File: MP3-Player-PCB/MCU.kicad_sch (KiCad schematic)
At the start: 24 parts, among them J101 Conn_ARM_SWD_TagConnect_TC2030, U101 STM32F411CEUx, Y101 8MHz

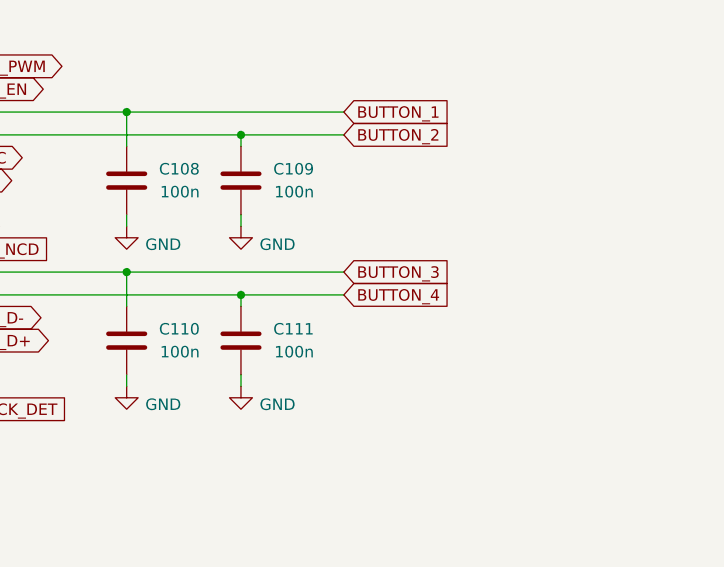
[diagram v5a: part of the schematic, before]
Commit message: Routed button gpio signals
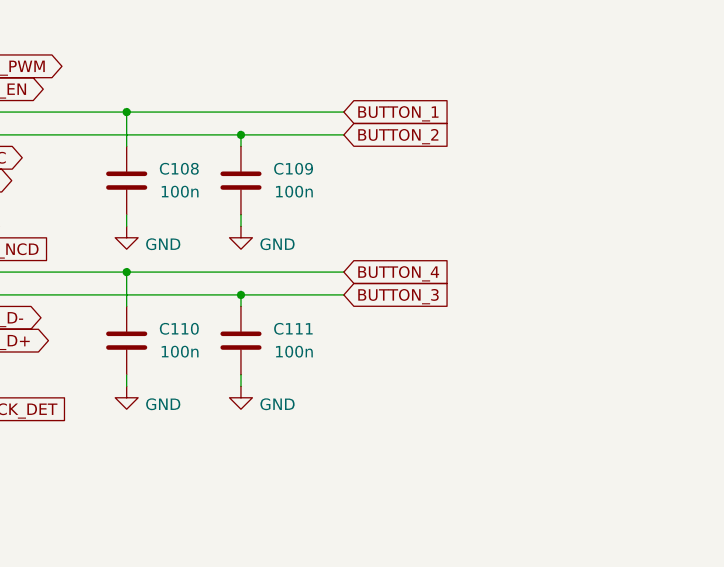
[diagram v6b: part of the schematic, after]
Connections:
- net BUTTON_3: now also C111.1, U101.31 (PA10); no longer C110.1, U101.30 (PA9)
- net BUTTON_4: now also C110.1, U101.30 (PA9); no longer C111.1, U101.31 (PA10)
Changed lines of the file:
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@@
-		)
-	)
-	(global_label "BUTTON_3"
-		(shape input)
-		(at 233.68 83.82 0)
-		(fields_autoplaced yes)
-		(effects
-			(font
-				(size 1.27 1.27)
-			)
-			(justify left)
-		)
-		(property "Intersheetrefs" "${INTERSHEET_REFS}"
-			(at 246.039 83.82 0)
-			(effects
-				(font
-					(size 1.27 1.27)
-				)
-				(justify left)
-				(hide yes)
-			)
 		)
 	)
@@
 		)
 	)
+	(global_label "SD_CARD_NCD"
+		(shape input)
+		(at 185.42 81.28 0)
+		(fields_autoplaced yes)
+		(effects
+			(font
+				(size 1.27 1.27)
+			)
+			(justify left)
+		)
+		(property "Intersheetrefs" "${INTERSHEET_REFS}"
+			(at 201.589 81.28 0)
+			(effects
+				(font
+					(size 1.27 1.27)
+				)
+				(justify left)
+				(hide yes)
+			)
+		)
+	)
+	(global_label "DAC_DIN"
+		(shape output)
+		(at 185.42 78.74 0)
+		(fields_autoplaced yes)
+		(effects
+			(font
+				(size 1.27 1.27)
+			)
+			(justify left)
+		)
+		(property "Intersheetrefs" "${INTERSHEET_REFS}"
+			(at 196.2067 78.74 0)
+			(effects
+				(font
+					(size 1.27 1.27)
+				)
+				(justify left)
+				(hide yes)
+			)
+		)
+	)
+	(global_label "DAC_GPO"
+		(shape input)
+		(at 129.54 81.28 180)
+		(fields_autoplaced yes)
+		(effects
+			(font
+				(size 1.27 1.27)
+			)
+			(justify right)
+		)
+		(property "Intersheetrefs" "${INTERSHEET_REFS}"
+			(at 118.0881 81.28 0)
+			(effects
+				(font
+					(size 1.27 1.27)
+				)
+				(justify right)
+				(hide yes)
+			)
+		)
+	)
+	(global_label "LEDS_PWR_EN"
+		(shape output)
+		(at 185.42 63.5 0)
+		(fields_autoplaced yes)
+		(effects
+			(font
+				(size 1.27 1.27)
+			)
+			(justify left)
+		)
+		(property "Intersheetrefs" "${INTERSHEET_REFS}"
+			(at 201.4679 63.5 0)
+			(effects
+				(font
+					(size 1.27 1.27)
+				)
+				(justify left)
+				(hide yes)
+			)
+		)
+	)
+	(global_label "AUDIO_JACK_DET"
+		(shape input)
+		(at 185.42 99.06 0)
+		(fields_autoplaced yes)
+		(effects
+			(font
+				(size 1.27 1.27)
+			)
+			(justify left)
+		)
+		(property "Intersheetrefs" "${INTERSHEET_REFS}"
+			(at 203.9476 99.06 0)
+			(effects
+				(font
+					(size 1.27 1.27)
+				)
+				(justify left)
+				(hide yes)
+			)
+		)
+	)
 	(global_label "BUTTON_4"
 		(shape input)
-		(at 233.68 86.36 0)
-		(fields_autoplaced yes)
-		(effects
-			(font
-				(size 1.27 1.27)
-			)
-			(justify left)
-		)
-		(property "Intersheetrefs" "${INTERSHEET_REFS}"
-			(at 246.039 86.36 0)
-			(effects
-				(font
-					(size 1.27 1.27)
-				)
-				(justify left)
-				(hide yes)
-			)
-		)
-	)
-	(global_label "SD_CARD_NCD"
-		(shape input)
-		(at 185.42 81.28 0)
-		(fields_autoplaced yes)
-		(effects
-			(font
-				(size 1.27 1.27)
-			)
-			(justify left)
-		)
-		(property "Intersheetrefs" "${INTERSHEET_REFS}"
-			(at 201.589 81.28 0)
-			(effects
-				(font
-					(size 1.27 1.27)
-				)
-				(justify left)
-				(hide yes)
-			)
-		)
-	)
-	(global_label "DAC_DIN"
-		(shape output)
-		(at 185.42 78.74 0)
-		(fields_autoplaced yes)
-		(effects
-			(font
-				(size 1.27 1.27)
-			)
-			(justify left)
-		)
-		(property "Intersheetrefs" "${INTERSHEET_REFS}"
-			(at 196.2067 78.74 0)
-			(effects
-				(font
-					(size 1.27 1.27)
-				)
-				(justify left)
-				(hide yes)
-			)
-		)
-	)
-	(global_label "DAC_GPO"
-		(shape input)
-		(at 129.54 81.28 180)
-		(fields_autoplaced yes)
-		(effects
-			(font
-				(size 1.27 1.27)
-			)
-			(justify right)
-		)
-		(property "Intersheetrefs" "${INTERSHEET_REFS}"
-			(at 118.0881 81.28 0)
-			(effects
-				(font
-					(size 1.27 1.27)
-				)
-				(justify right)
-				(hide yes)
-			)
-		)
-	)
-	(global_label "LEDS_PWR_EN"
-		(shape output)
-		(at 185.42 63.5 0)
-		(fields_autoplaced yes)
-		(effects
-			(font
-				(size 1.27 1.27)
-			)
-			(justify left)
-		)
-		(property "Intersheetrefs" "${INTERSHEET_REFS}"
-			(at 201.4679 63.5 0)
-			(effects
-				(font
-					(size 1.27 1.27)
-				)
-				(justify left)
-				(hide yes)
-			)
-		)
-	)
-	(global_label "AUDIO_JACK_DET"
-		(shape input)
-		(at 185.42 99.06 0)
-		(fields_autoplaced yes)
-		(effects
-			(font
-				(size 1.27 1.27)
-			)
-			(justify left)
-		)
-		(property "Intersheetrefs" "${INTERSHEET_REFS}"
-			(at 203.9476 99.06 0)
+		(at 233.68 83.82 0)
+		(fields_autoplaced yes)
+		(effects
+			(font
+				(size 1.27 1.27)
+			)
+			(justify left)
+		)
+		(property "Intersheetrefs" "${INTERSHEET_REFS}"
+			(at 246.039 83.82 0)
 			(effects
 				(font
@@
 				(hide yes)
 			)
+		)
+	)
+	(global_label "BUTTON_3"
+		(shape input)
+		(at 233.68 86.36 0)
+		(fields_autoplaced yes)
+		(effects
+			(font
+				(size 1.27 1.27)
+			)
+			(justify left)
+		)
+		(property "Intersheetrefs" "${INTERSHEET_REFS}"
+			(at 246.039 86.36 0)
+			(effects
+				(font
+					(size 1.27 1.27)
+				)
+				(justify left)
+				(hide yes)
+			)

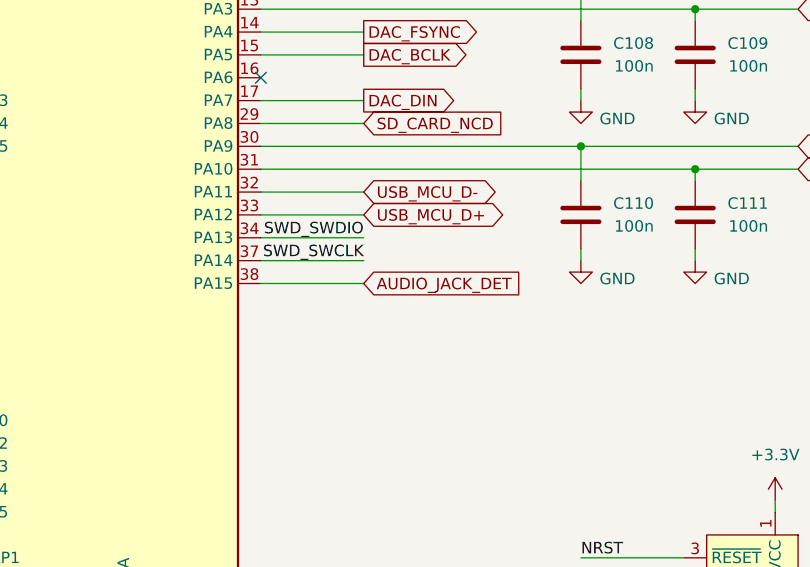
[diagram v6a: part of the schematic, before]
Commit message: Finished Audio Jack routing
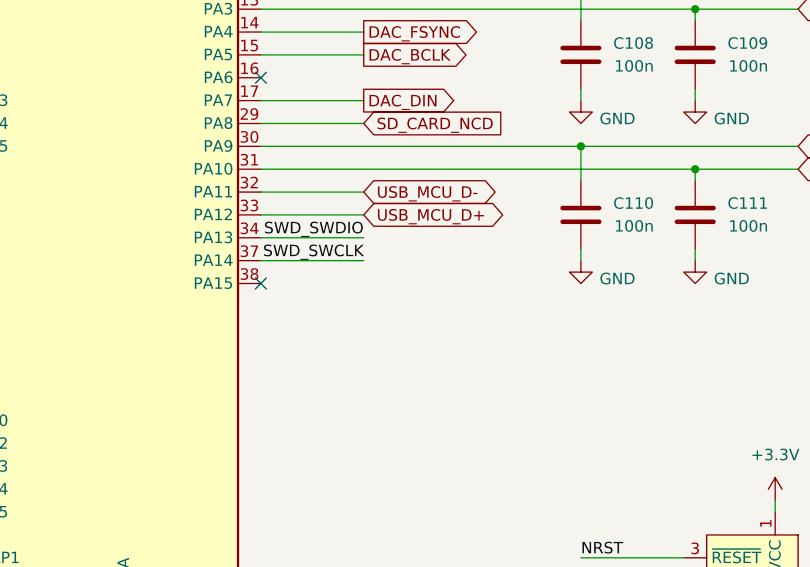
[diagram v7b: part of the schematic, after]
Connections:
- net AUDIO_JACK_DET: no longer names the net of U101.38 (PA15)
- no-connect marks 4 -> 5
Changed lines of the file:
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@@
+	)
+	(no_connect
+		(at 173.99 99.06)
 	)
 	(no_connect
@@
 		(pts
 			(xy 105.41 48.26) (xy 105.41 50.8)
-		)
-		(stroke
-			(width 0)
-			(type default)
-		)
-	)
-	(wire
-		(pts
-			(xy 185.42 99.06) (xy 173.99 99.06)
 		)
 		(stroke
@@
 			(effects
 				(font
-					(size 1.27 1.27)
-				)
-				(justify left)
-				(hide yes)
-			)
-		)
-	)
-	(global_label "AUDIO_JACK_DET"
-		(shape input)
-		(at 185.42 99.06 0)
-		(fields_autoplaced yes)
-		(effects
-			(font
-				(size 1.27 1.27)
-			)
-			(justify left)
-		)
-		(property "Intersheetrefs" "${INTERSHEET_REFS}"
-			(at 203.9476 99.06 0)
-			(effects
-				(font

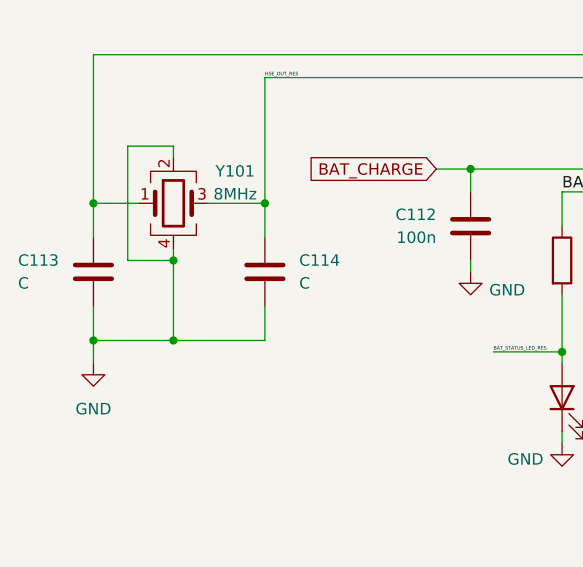
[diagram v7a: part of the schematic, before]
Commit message: Assigning JLCPCB part #'s
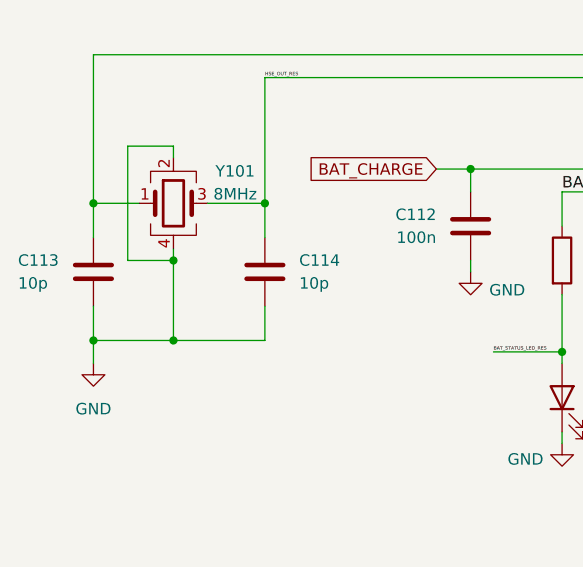
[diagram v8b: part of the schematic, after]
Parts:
- C101, C115: JLCPCB Part # (none) -> C1705
- C102, C103, C104, C105, C106, C107, C108, C109, C110, C111, C112: JLCPCB Part # (none) -> C1525
- C113, C114: value C -> 10p; JLCPCB Part # (none) -> C162202
- R101: JLCPCB Part # (none) -> C25531
- R102: JLCPCB Part # (none) -> C15402
- U101: JLCPCB Part # (none) -> C2054095
- Y101: JLCPCB Part # (none) -> C518154
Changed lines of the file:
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@@
+			)
+		)
+		(property "JLCPCB Part #" "C1525"
+			(at 105.41 44.45 0)
+			(effects
+				(font
+					(size 1.27 1.27)
+				)
+				(hide yes)
 			)
 		)
@@
 			)
 		)
+		(property "JLCPCB Part #" ""
+			(at 113.03 99.06 0)
+			(effects
+				(font
+					(size 1.27 1.27)
+				)
+				(hide yes)
+			)
+		)
 		(pin "2"
 		)
@@
 		)
 		(property "Description" "Four pin crystal, GND on pins 2 and 4"
+			(at 55.88 92.71 0)
+			(effects
+				(font
+					(size 1.27 1.27)
+				)
+				(hide yes)
+			)
+		)
+		(property "JLCPCB Part #" "C518154"
 			(at 55.88 92.71 0)
 			(effects
@@
 			)
 		)
+		(property "JLCPCB Part #" ""
+			(at 99.06 114.3 90)
+			(effects
+				(font
+					(size 1.27 1.27)
+				)
+				(hide yes)
+			)
+		)
 		(pin "2"
 		)
@@
 			)
 		)
+		(property "JLCPCB Part #" "C1525"
+			(at 88.9 95.25 0)
+			(effects
+				(font
+					(size 1.27 1.27)
+				)
+				(hide yes)
+			)
+		)
 		(pin "2"
 		)
@@
 		(property "Description" "Resistor"
 			(at 129.54 66.04 0)
+			(effects
+				(font
+					(size 1.27 1.27)
+				)
+				(hide yes)
+			)
+		)
+		(property "JLCPCB Part #" "C25531"
+			(at 129.54 66.04 90)
 			(effects
 				(font
@@
 			)
 		)
+		(property "JLCPCB Part #" "C2054095"
+			(at 156.21 96.52 0)
+			(effects
+				(font
+					(size 1.27 1.27)
+				)
+				(hide yes)
+			)
+		)
 		(pin "20"
 		)
@@
 			)
 		)
+		(property "JLCPCB Part #" ""
+			(at 99.06 99.06 0)
+			(effects
+				(font
+					(size 1.27 1.27)
+				)
+				(hide yes)
+			)
+		)
 		(pin "2"
 		)
@@
 			)
 		)
+		(property "JLCPCB Part #" "C1525"
+			(at 222.25 91.44 0)
+			(effects
+				(font
+					(size 1.27 1.27)
+				)
+				(hide yes)
+			)
+		)
 		(pin "2"
 		)
@@
 			)
 		)
+		(property "JLCPCB Part #" "C1525"
+			(at 139.7 44.45 0)
+			(effects
+				(font
+					(size 1.27 1.27)
+				)
+				(hide yes)
+			)
+		)
 		(pin "2"
 		)
@@
 			)
 		)
+		(property "JLCPCB Part #" ""
+			(at 228.6 134.62 0)
+			(effects
+				(font
+					(size 1.27 1.27)
+				)
+				(hide yes)
+			)
+		)
 		(pin "4"
 		)
@@
 			)
 		)
-		(property "Value" "C"
+		(property "Value" "10p"
 			(at 69.85 101.5999 0)
 			(effects
@@
 		)
 		(property "Description" "Unpolarized capacitor"
+			(at 66.04 100.33 0)
+			(effects
+				(font
+					(size 1.27 1.27)
+				)
+				(hide yes)
+			)
+		)
+		(property "JLCPCB Part #" "C162202"
 			(at 66.04 100.33 0)
 			(effects
@@
 			)
 		)
+		(property "JLCPCB Part #" "C15402"
+			(at 124.46 78.74 90)
+			(effects
+				(font
+					(size 1.27 1.27)
+				)
+				(hide yes)
+			)
+		)
 		(pin "1"
 		)
@@
 			)
 		)
+		(property "JLCPCB Part #" "C1525"
+			(at 209.55 91.44 0)
+			(effects
+				(font
+					(size 1.27 1.27)
+				)
+				(hide yes)
+			)
+		)
 		(pin "2"
 		)
@@
 			)
 		)
+		(property "JLCPCB Part #" "C1525"
+			(at 128.27 44.45 0)
+			(effects
+				(font
+					(size 1.27 1.27)
+				)
+				(hide yes)
+			)
+		)
 		(pin "2"
 		)
@@
 			)
 		)
+		(property "JLCPCB Part #" "C1525"
+			(at 209.55 73.66 0)
+			(effects
+				(font
+					(size 1.27 1.27)
+				)
+				(hide yes)
+			)
+		)
 		(pin "2"
 		)
@@
 			)
 		)
+		(property "JLCPCB Part #" "C1525"
+			(at 93.98 44.45 0)
+			(effects
+				(font
+					(size 1.27 1.27)
+				)
+				(hide yes)
+			)
+		)
 		(pin "2"
 		)
@@
 			)
 		)
+		(property "JLCPCB Part #" "C1705"
+			(at 127 134.62 0)
+			(effects
+				(font
+					(size 1.27 1.27)
+				)
+				(hide yes)
+			)
+		)
 		(pin "2"
 		)
@@
 			)
 		)
+		(property "JLCPCB Part #" "C1525"
+			(at 116.84 44.45 0)
+			(effects
+				(font
+					(size 1.27 1.27)
+				)
+				(hide yes)
+			)
+		)
 		(pin "2"
 		)
@@
 			)
 		)
-		(property "Value" "C"
+		(property "Value" "10p"
 			(at 38.608 101.6 0)
 			(effects
@@
 		)
 		(property "Description" "Unpolarized capacitor"
+			(at 46.99 100.33 0)
+			(effects
+				(font
+					(size 1.27 1.27)
+				)
+				(hide yes)
+			)
+		)
+		(property "JLCPCB Part #" "C162202"
 			(at 46.99 100.33 0)
 			(effects
@@
 			)
 		)
+		(property "JLCPCB Part #" "C1705"
+			(at 82.55 44.45 0)
+			(effects
+				(font
+					(size 1.27 1.27)
+				)
+				(hide yes)
+			)
+		)
 		(pin "2"
 		)
@@
 		)
 		(property "Description" "Unpolarized capacitor"
+			(at 118.11 67.31 0)
+			(effects
+				(font
+					(size 1.27 1.27)
+				)
+				(hide yes)
+			)
+		)
+		(property "JLCPCB Part #" "C1525"
 			(at 118.11 67.31 0)
 			(effects
@@
 			)
 		)
+		(property "JLCPCB Part #" "C1525"
+			(at 222.25 73.66 0)
+			(effects
+				(font
+					(size 1.27 1.27)
+				)
+				(hide yes)
+			)
+		)
 		(pin "2"
 		)
@@
 			(effects
 				(font
+					(size 1.27 1.27)
+				)
+				(hide yes)
+			)
+		)
+		(property "JLCPCB Part #" ""
+			(at 113.03 114.3 90)
+			(effects
+				(font
